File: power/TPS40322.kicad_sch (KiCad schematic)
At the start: 68 parts, among them U5 TPS40322RHBR, U6 CSD86330Q3D, U7 CSD86330Q3D

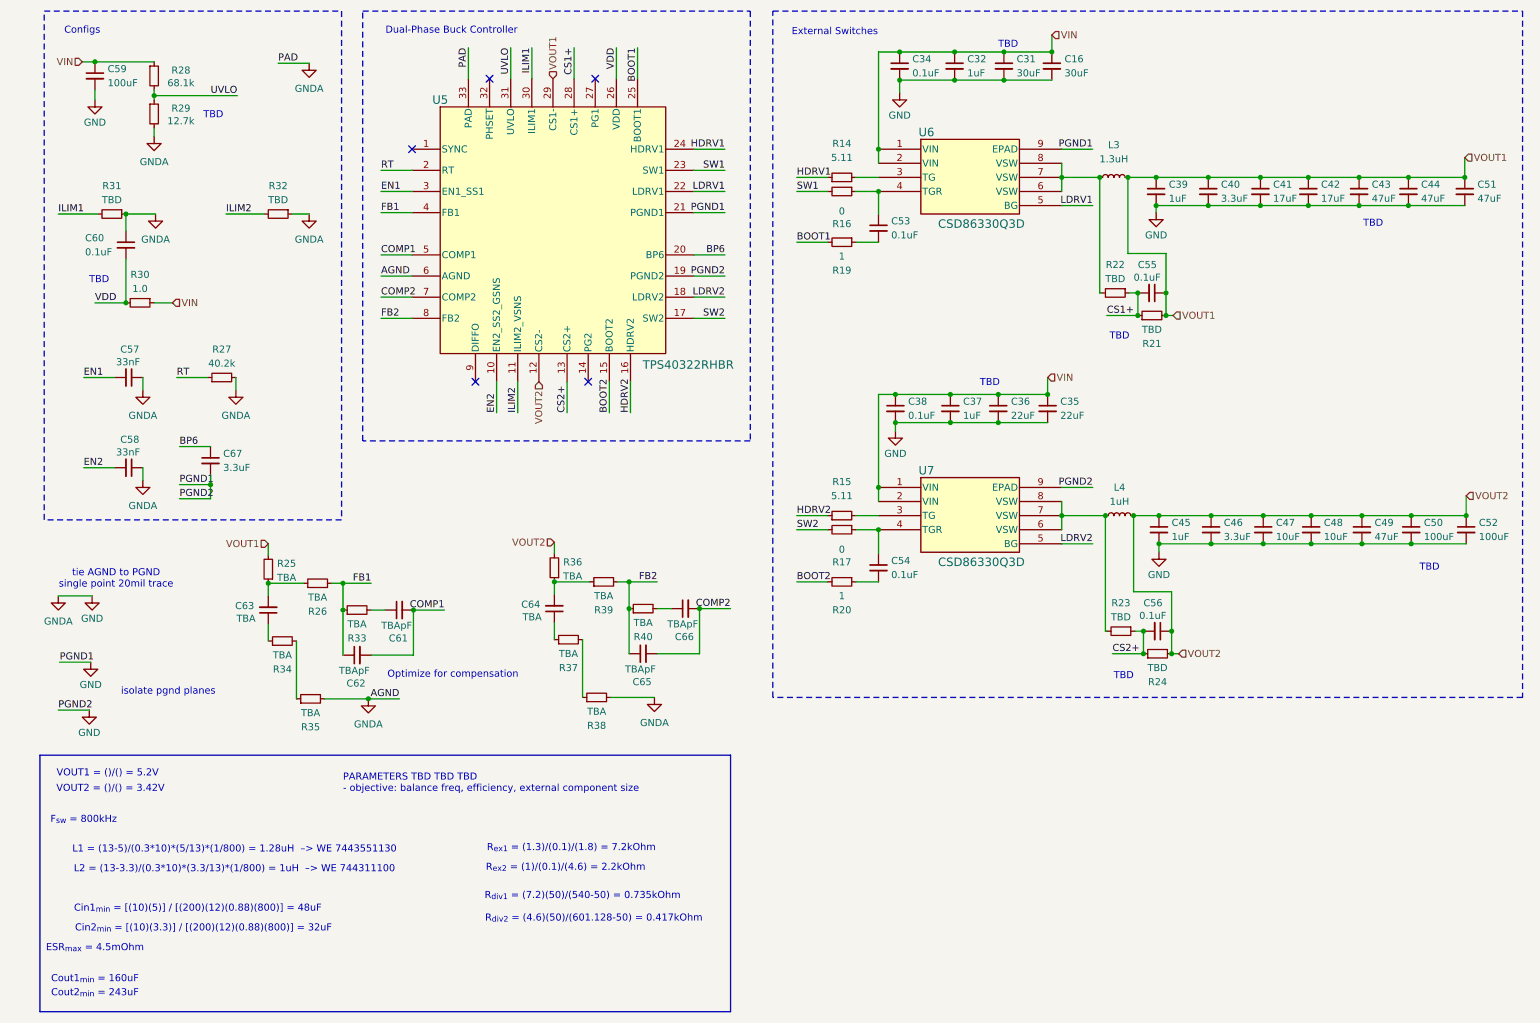
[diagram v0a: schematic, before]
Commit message: Feat[power]: finished dual buck ic sheet
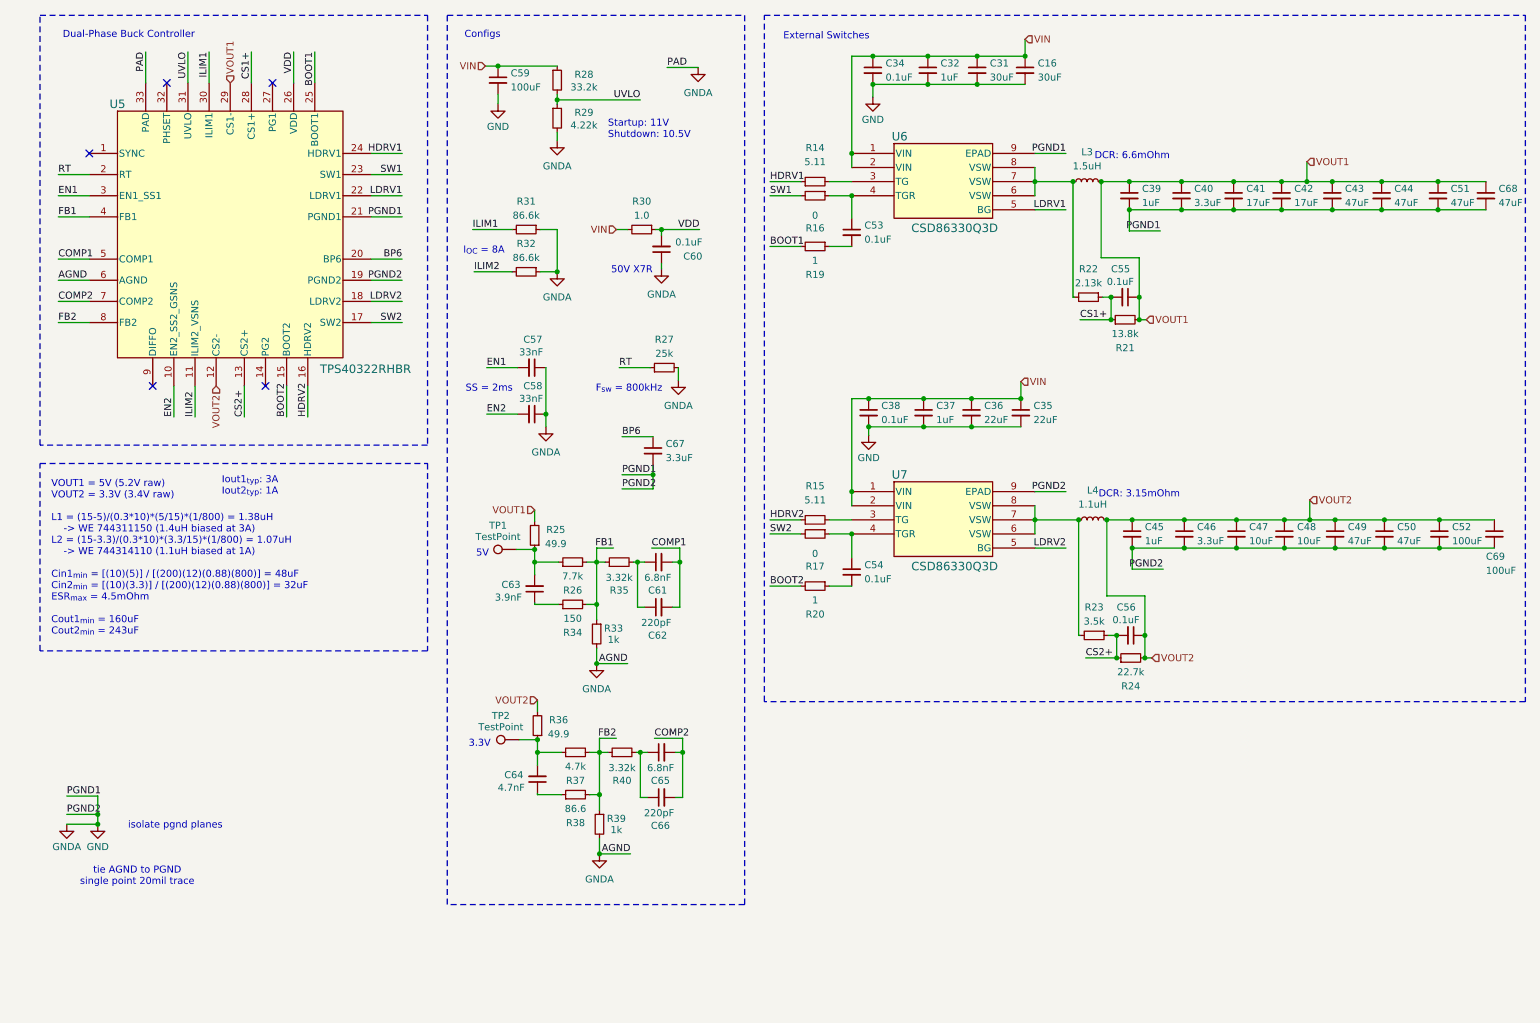
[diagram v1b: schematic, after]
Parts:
- added C68: 47uF, symbol Device:C_Small
- added C69: 100uF, symbol Device:C_Small
- added TP1, TP2: TestPoint, symbol Connector:TestPoint
- C50: value 100uF -> 47uF
- C61, C65: value TBApF -> 6.8nF
- C62, C66: value TBApF -> 220pF
- C63: value TBA -> 3.9nF
- C64: value TBA -> 4.7nF
- L3: value 1.3uH -> 1.5uH
- L4: value 1uH -> 1.1uH
- R21: value TBD -> 13.8k
- R22: value TBD -> 2.13k
- R23: value TBD -> 3.5k
- R24: value TBD -> 22.7k
- R25, R36: value TBA -> 49.9
- R26: value TBA -> 7.7k
- R27: value 40.2k -> 25k
- R28: value 68.1k -> 33.2k
- R29: value 12.7k -> 4.22k
- R31, R32: value TBD -> 86.6k
- R33, R39: value TBA -> 1k
- R34: value TBA -> 150
- R35, R40: value TBA -> 3.32k
- R37: value TBA -> 4.7k
- R38: value TBA -> 86.6
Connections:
- net FB1: now also R34.2, R35.1; no longer C62.1
- net FB2: now also R37.2, R38.2, R39.1; no longer C65.1, R39.2
- net GND: now also R33.2, R39.2, C68.2, C69.2; no longer R35.2, R38.2
- net VDD: now also R30.1; no longer R30.2
- net VIN: now also R30.2; no longer R30.1
- net VOUT1: now also C68.1
- net VOUT2: now also C69.1
- net at C61.1: now also C62.1, R35.2; no longer R33.2
- net at C66.1, R40.2: now also C65.1
- net at C64.2, R36.1: now also R37.1, TP2.1; no longer R39.1
- net at R38.1: now also C64.1; no longer R37.2
- net at C63.2, R25.1, R26.1: now also TP1.1
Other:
- note added: "3.3V"
- note added: "50V X7R"
- note added: "5V"
- note added: "DCR: 3.15mOhm"
- note added: "DCR: 6.6mOhm"
- note added: "I_{OC} = 8A"
- note added: "Iout1_{typ}: 3A Iout2_{typ}: 1A"
- note added: "SS = 2ms"
- note added: "Startup: 11V Shutdown: 10.5V"
- note added: "VOUT1 = 5V (5.2V raw) VOUT2 = 3.3V (3.4V raw) L1 = (15-5)/(0.3*10)*(5/15)*(1/800) = 1.38uH -> WE 744311150 (1.4uH biased at 3A) L2 = (15-3.3)/(0.3*10)*(3.3/15)*(1/800) = 1.07uH -> WE 744314110 (1.1uH biased at 1A) Cin1_{min} = [(10)(5)] / [(200)(12)(0.88)(800)] = 48uF Cin2_{min} = [(10)(3.3)] / [(200)(12)(0.88)(800)] = 32uF ESR_{max} = 4.5mOhm Cout1_{min} = 160uF Cout2_{min} = 243uF"
- note removed: "Cin1_{min} = [(10)(5)] / [(200)(12)(0.88)(800)] = 48uF"
- note removed: "Cin2_{min} = [(10)(3.3)] / [(200)(12)(0.88)(800)] = 32uF"
- note removed: "Cout1_{min} = 160uF"
- note removed: "Cout2_{min} = 243uF"
- note removed: "ESR_{max} = 4.5mOhm"
- note removed: "L1 = (13-5)/(0.3*10)*(5/13)*(1/800) = 1.28uH –> WE 7443551130"
- note removed: "L2 = (13-3.3)/(0.3*10)*(3.3/13)*(1/800) = 1uH –> WE 744311100"
- note removed: "Optimize for compensation"
- note removed: "PARAMETERS TBD TBD TBD - objective: balance freq, efficiency, external component size"
- note removed: "R_{div1} = (7.2)(50)/(540-50) = 0.735kOhm"
- note removed: "R_{div2} = (4.6)(50)/(601.128-50) = 0.417kOhm"
- note removed: "R_{ex1} = (1.3)/(0.1)/(1.8) = 7.2kOhm"
- note removed: "R_{ex2} = (1)/(0.1)/(4.6) = 2.2kOhm"
- note removed: "TBD"
- note removed: "VOUT1 = ()/() = 5.2V"
- note removed: "VOUT2 = ()/() = 3.42V"
- moved on the sheet: C16, C31, C32, C34, C35, C36, C37, C38, C39, C40, C41, C42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

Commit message: Feat[power]: v2 schematic draft complete
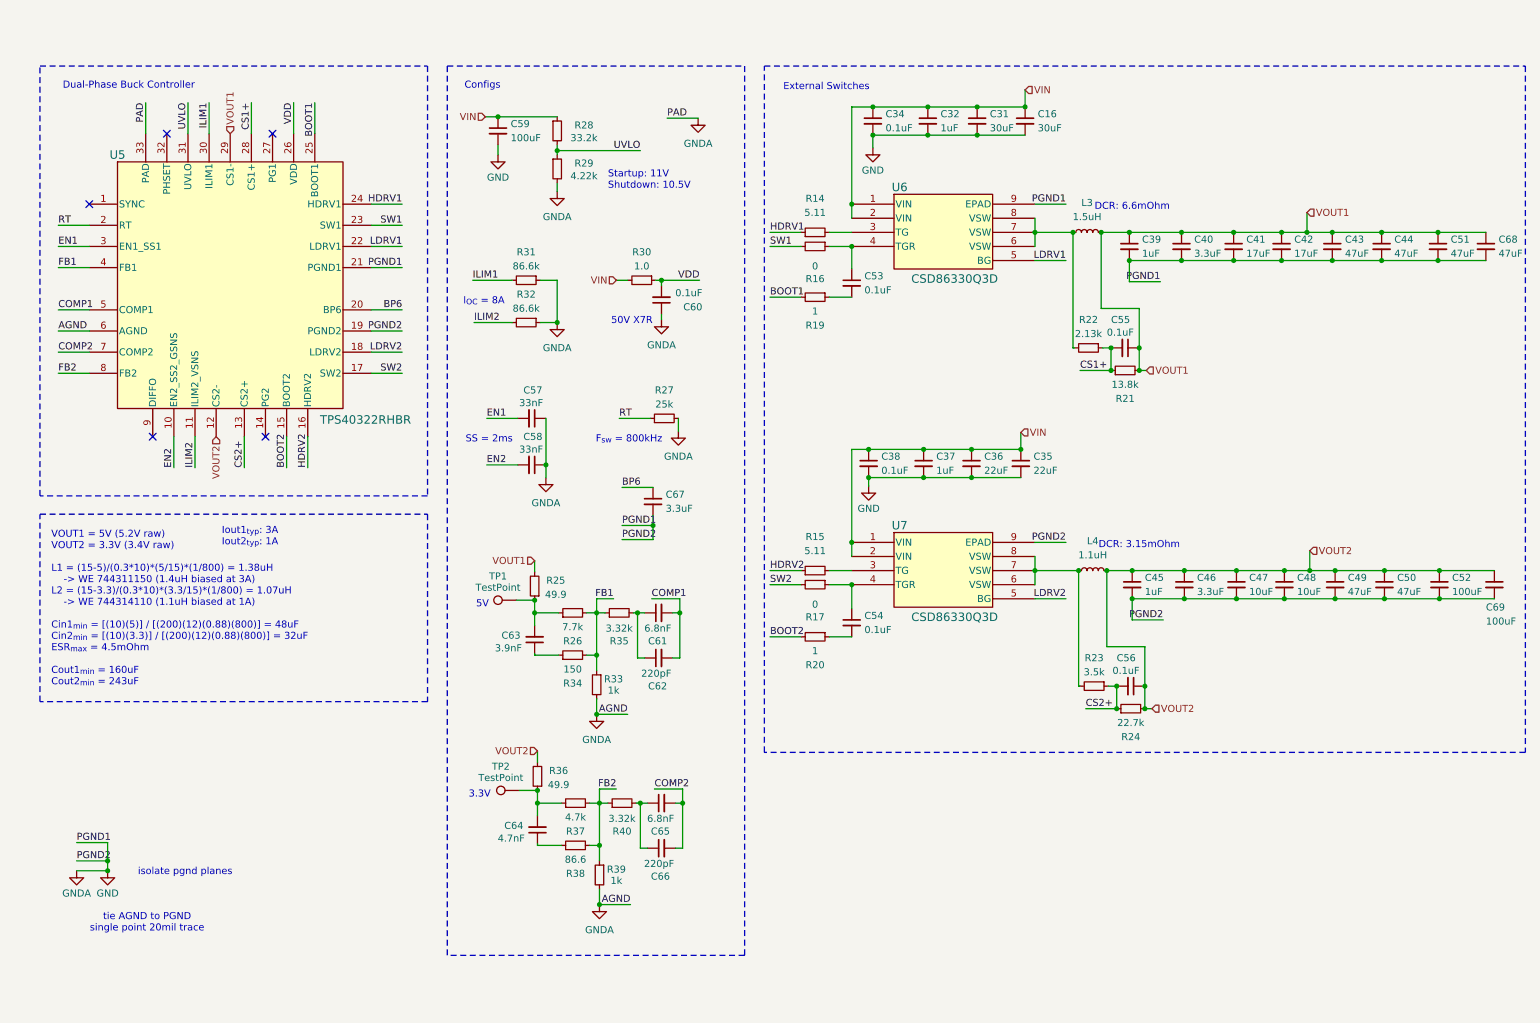
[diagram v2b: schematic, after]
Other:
- company: (none) -> MUREX Robotics [Max Liu]
- title: (none) -> Power Board
- moved on the sheet: C16, C31, C32, C34, C35, C36, C37, C38, C39, C40, C41, C42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

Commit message: Feat[power]: footprints assigned, initial layout
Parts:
- C1: renamed from C59; footprint (none) -> Capacitor_SMD:C_1206_3216Metric
- C10: renamed from C65; footprint (none) -> Capacitor_SMD:C_0603_1608Metric
- C11: renamed from C66; footprint (none) -> Capacitor_SMD:C_0603_1608Metric
- C12: renamed from C53; footprint (none) -> Capacitor_SMD:C_0603_1608Metric
- C13: renamed from C54; footprint (none) -> Capacitor_SMD:C_0603_1608Metric
- C14: renamed from C38; footprint (none) -> Capacitor_SMD:C_0603_1608Metric
- C15: renamed from C34; footprint (none) -> Capacitor_SMD:C_0603_1608Metric
- C16: renamed from C37; footprint (none) -> Capacitor_SMD:C_0603_1608Metric
- C17: renamed from C32; footprint (none) -> Capacitor_SMD:C_0603_1608Metric
- C18: renamed from C36; footprint (none) -> Capacitor_SMD:C_0603_1608Metric
- C19: renamed from C31; footprint (none) -> Capacitor_SMD:C_0603_1608Metric
- C2: renamed from C57; footprint (none) -> Capacitor_SMD:C_0603_1608Metric
- C20: renamed from C35; footprint (none) -> Capacitor_SMD:C_0603_1608Metric
- C21: renamed from C16; footprint (none) -> Capacitor_SMD:C_0603_1608Metric
- C22: renamed from C55; footprint (none) -> Capacitor_SMD:C_0603_1608Metric
- C23: renamed from C39; footprint (none) -> Capacitor_SMD:C_0603_1608Metric
- C24: renamed from C56; footprint (none) -> Capacitor_SMD:C_0603_1608Metric
- C25: renamed from C45; footprint (none) -> Capacitor_SMD:C_0603_1608Metric
- C26: renamed from C40; footprint (none) -> Capacitor_SMD:C_0603_1608Metric
- C27: renamed from C46; footprint (none) -> Capacitor_SMD:C_0603_1608Metric
- C28: renamed from C41; footprint (none) -> Capacitor_SMD:C_0603_1608Metric
- C29: renamed from C47; footprint (none) -> Capacitor_SMD:C_0603_1608Metric
- C3: renamed from C58; footprint (none) -> Capacitor_SMD:C_0603_1608Metric
- C30: renamed from C42; footprint (none) -> Capacitor_SMD:C_0603_1608Metric
- C31: renamed from C48; footprint (none) -> Capacitor_SMD:C_0603_1608Metric
- C32: renamed from C43; footprint (none) -> Capacitor_SMD:C_0805_2012Metric
- C33: renamed from C49; footprint (none) -> Capacitor_SMD:C_0805_2012Metric
- C34: renamed from C44; footprint (none) -> Capacitor_SMD:C_0805_2012Metric
- C35: renamed from C50; footprint (none) -> Capacitor_SMD:C_0805_2012Metric
- C36: renamed from C51; footprint (none) -> Capacitor_SMD:C_0805_2012Metric
- C37: renamed from C52; footprint (none) -> Capacitor_SMD:C_1206_3216Metric
- C38: renamed from C68; footprint (none) -> Capacitor_SMD:C_0805_2012Metric
- C39: renamed from C69; footprint (none) -> Capacitor_SMD:C_1206_3216Metric
- C4: renamed from C63; footprint (none) -> Capacitor_SMD:C_0603_1608Metric
- C5: renamed from C64; footprint (none) -> Capacitor_SMD:C_0603_1608Metric
- C6: renamed from C67; footprint (none) -> Capacitor_SMD:C_0603_1608Metric
- C7: renamed from C61; footprint (none) -> Capacitor_SMD:C_0603_1608Metric
- C8: renamed from C62; footprint (none) -> Capacitor_SMD:C_0603_1608Metric
- C9: renamed from C60; footprint (none) -> Capacitor_SMD:C_0603_1608Metric
- L1: renamed from L3; footprint (none) -> Power:WE-HCI_7030_7040_705023
- L2: renamed from L4; footprint (none) -> Power:WE-HCI_7030_7040_705023
- R10: renamed from R34; footprint (none) -> Resistor_SMD:R_0603_1608Metric
- R11: renamed from R37; footprint (none) -> Resistor_SMD:R_0603_1608Metric
- R12: renamed from R38; footprint (none) -> Resistor_SMD:R_0603_1608Metric
- R13: renamed from R33; footprint (none) -> Resistor_SMD:R_0603_1608Metric
- R14: renamed from R39; footprint (none) -> Resistor_SMD:R_0603_1608Metric
- R15: renamed from R35; footprint (none) -> Resistor_SMD:R_0603_1608Metric
- R16: renamed from R40; footprint (none) -> Resistor_SMD:R_0603_1608Metric
- R17: renamed from R30; footprint (none) -> Resistor_SMD:R_0603_1608Metric
- R18: renamed from R27; footprint (none) -> Resistor_SMD:R_0603_1608Metric
- R19: renamed from R14; footprint (none) -> Resistor_SMD:R_0603_1608Metric
- R20: renamed from R16; footprint (none) -> Resistor_SMD:R_0603_1608Metric
- R21: renamed from R19; footprint (none) -> Resistor_SMD:R_0603_1608Metric
- R22: renamed from R15; footprint (none) -> Resistor_SMD:R_0603_1608Metric
- R23: renamed from R17; footprint (none) -> Resistor_SMD:R_0603_1608Metric
- R24: renamed from R20; footprint (none) -> Resistor_SMD:R_0603_1608Metric
- R25: renamed from R22; footprint (none) -> Resistor_SMD:R_0603_1608Metric
- R26: renamed from R23; footprint (none) -> Resistor_SMD:R_0603_1608Metric
- R27: renamed from R21; footprint (none) -> Resistor_SMD:R_0603_1608Metric
- R28: renamed from R24; footprint (none) -> Resistor_SMD:R_0603_1608Metric
- R3: renamed from R31; footprint (none) -> Resistor_SMD:R_0603_1608Metric
- R4: renamed from R32; footprint (none) -> Resistor_SMD:R_0603_1608Metric
- R5: renamed from R25; footprint (none) -> Resistor_SMD:R_0603_1608Metric
- R6: renamed from R36; footprint (none) -> Resistor_SMD:R_0603_1608Metric
- R7: renamed from R28; footprint (none) -> Resistor_SMD:R_0603_1608Metric
- R8: renamed from R29; footprint (none) -> Resistor_SMD:R_0603_1608Metric
- R9: renamed from R26; footprint (none) -> Resistor_SMD:R_0603_1608Metric
- TP1, TP2: footprint (none) -> TestPoint:TestPoint_Pad_1.5x1.5mm
- U1: renamed from U5; footprint RHB0032D -> Power:RHB0032D
- U2: renamed from U6; footprint DQZ8_1P8X2P7 -> Power:DQZ8_1P8X2P7
- U3: renamed from U7; footprint DQZ8_1P8X2P7 -> Power:DQZ8_1P8X2P7
